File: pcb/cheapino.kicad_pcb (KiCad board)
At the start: 2 copper layers, 132.5 x 95.1 mm, 149 parts, among them J1 USB_C_Receptacle_USB2.0_16P, J2 DBG, J3 SJ-43514, K1 SW_Push, K10 SW_Push, K11 SW_Push, K12 SW_Push, K13 SW_Push, K14 SW_Push, K15 SW_Push, K16 SW_Push, K17 SW_Push, K18 SW_Push, K2 SW_Push, K3 SW_Push, K4 SW_Push, K5 SW_Push, K6 SW_Push, K7 SW_Push, K8 SW_Push, K9 SW_Push, SW1 BOOT, SW2 RST, U1 RP2040, U2 W25Q128JVSIQ, U3 AP2112K-3.3, U4 TVS0500DRV, U5 TPD2E2U06, U6 TPD2E2U06, U7 TXS0101DBV, U8 TXS0101DBV, Y1 12MHz

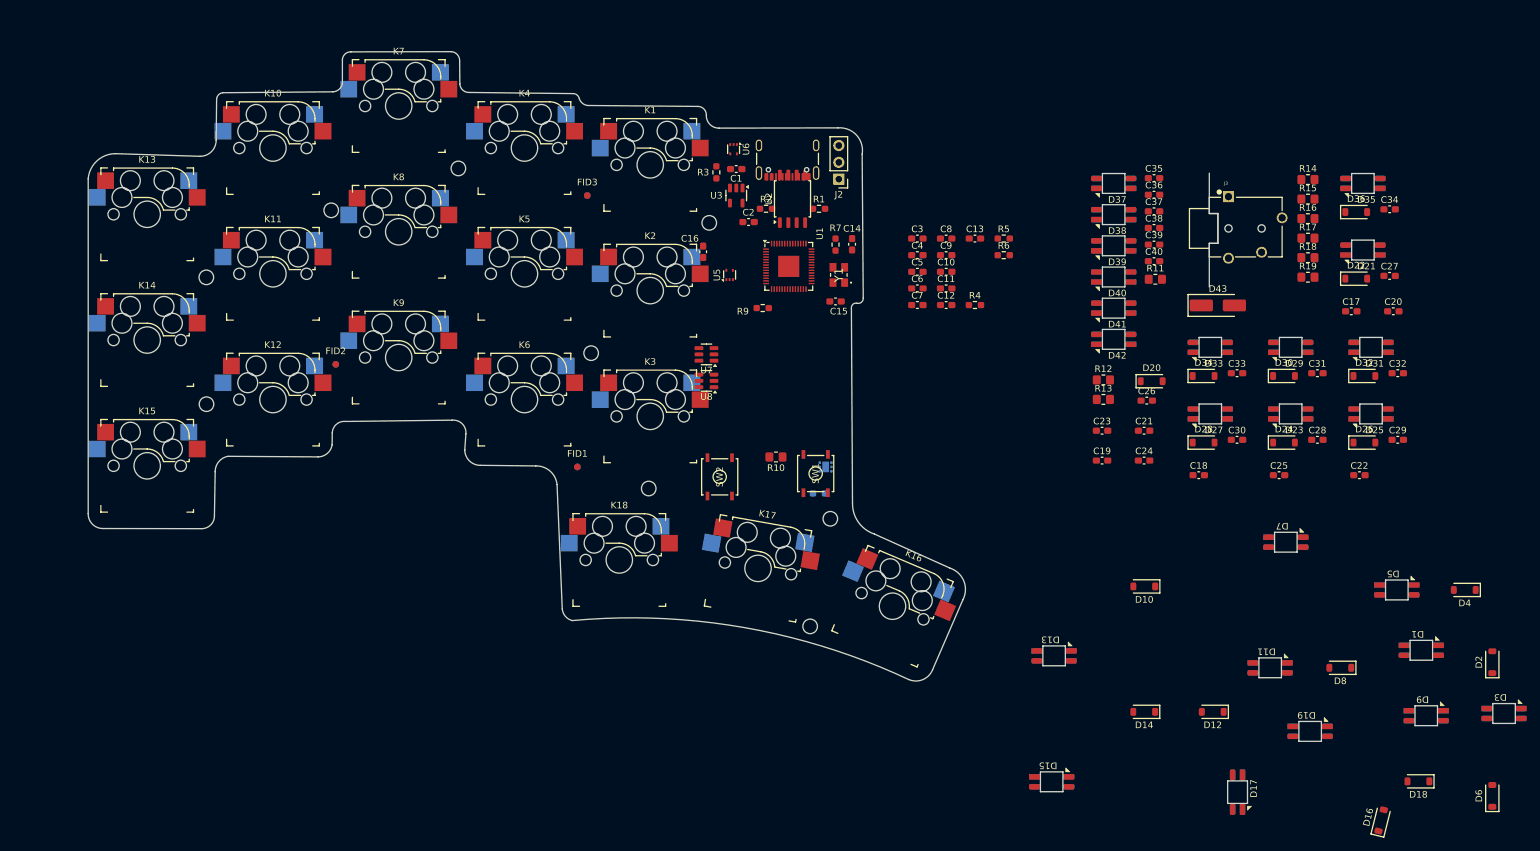
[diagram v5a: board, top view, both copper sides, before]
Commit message: Broke out Underglow LEDs into a common hierarchical sheet for what may be more consistent placements. Additionally created hierarchical PCB layouts and started using the HierarchicalPcb plugin (https://github.com/gauravmm/HierarchicalPcb.git) to automatically layout repeated components for the keymap.
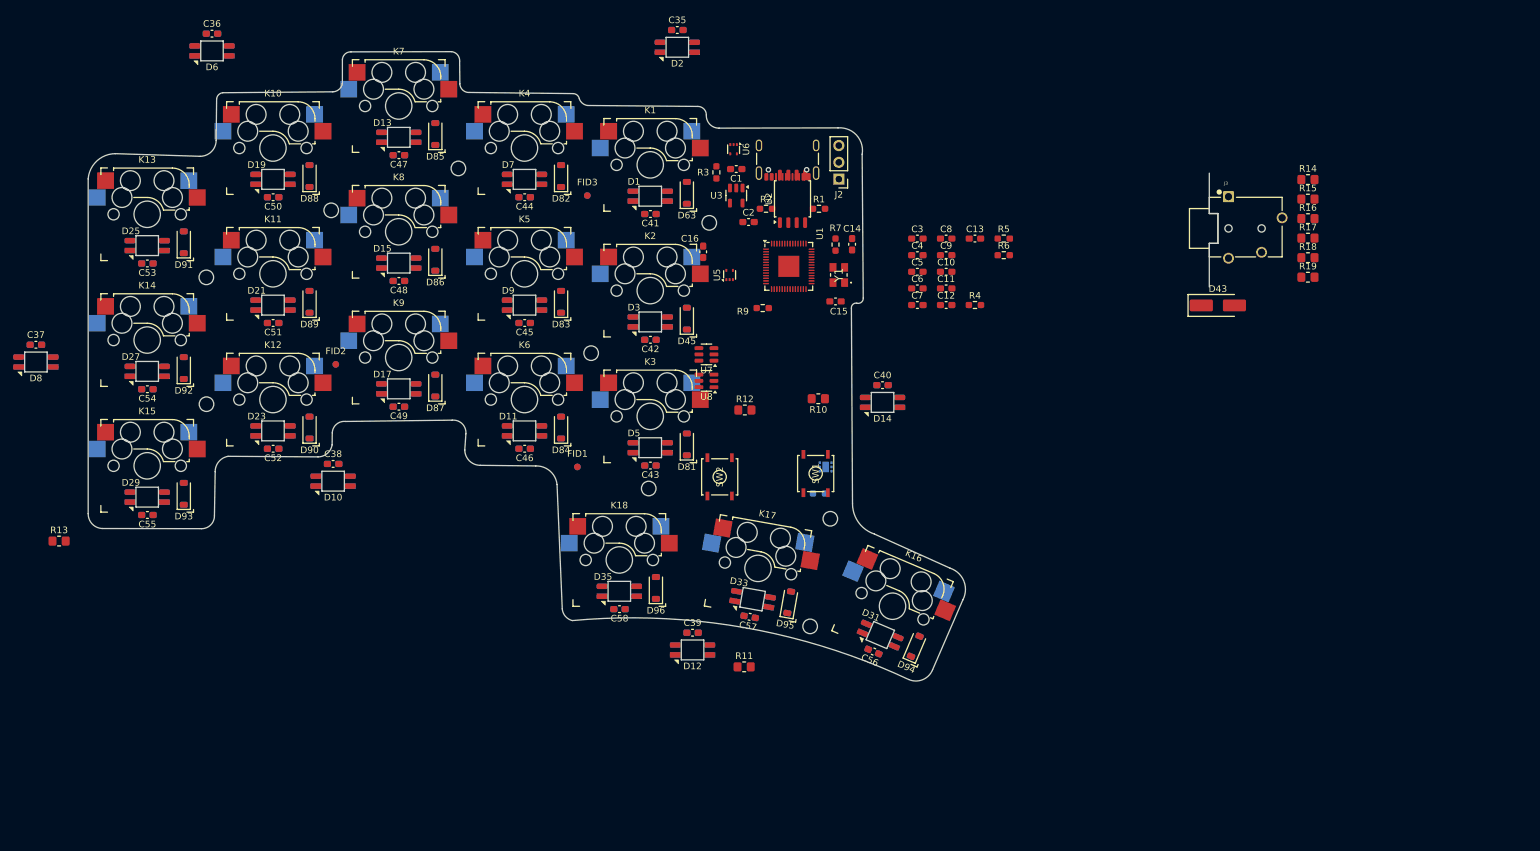
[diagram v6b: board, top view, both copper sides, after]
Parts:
- removed D16, D18, D20, D22, D24, D26, D28, D30, D32, D34, D36: 1N4148W, Diode_SMD:D_SOD-123
- removed D37, D38, D39, D40, D41, D42: ~, Extra:SK6812-MINI-E_ReverseMount_reversible
- added C41: 100nF, Capacitor_SMD:C_0603_1608Metric_Pad1.08x0.95mm_HandSolder, F.Cu at (145.0, 70.3)
- added C42: 100nF, Capacitor_SMD:C_0603_1608Metric_Pad1.08x0.95mm_HandSolder, F.Cu at (145.0, 89.3)
- added C43: 100nF, Capacitor_SMD:C_0603_1608Metric_Pad1.08x0.95mm_HandSolder, F.Cu at (145.0, 108.3)
- added C44: 100nF, Capacitor_SMD:C_0603_1608Metric_Pad1.08x0.95mm_HandSolder, F.Cu at (126.0, 67.8)
- added C45: 100nF, Capacitor_SMD:C_0603_1608Metric_Pad1.08x0.95mm_HandSolder, F.Cu at (126.0, 86.8)
- added C46: 100nF, Capacitor_SMD:C_0603_1608Metric_Pad1.08x0.95mm_HandSolder, F.Cu at (126.0, 105.8)
- added C47: 100nF, Capacitor_SMD:C_0603_1608Metric_Pad1.08x0.95mm_HandSolder, F.Cu at (107.0, 61.4)
- added C48: 100nF, Capacitor_SMD:C_0603_1608Metric_Pad1.08x0.95mm_HandSolder, F.Cu at (107.0, 80.4)
- added C49: 100nF, Capacitor_SMD:C_0603_1608Metric_Pad1.08x0.95mm_HandSolder, F.Cu at (107.0, 99.4)
- added C50: 100nF, Capacitor_SMD:C_0603_1608Metric_Pad1.08x0.95mm_HandSolder, F.Cu at (88.0, 67.8)
- added C51: 100nF, Capacitor_SMD:C_0603_1608Metric_Pad1.08x0.95mm_HandSolder, F.Cu at (88.0, 86.8)
- added C52: 100nF, Capacitor_SMD:C_0603_1608Metric_Pad1.08x0.95mm_HandSolder, F.Cu at (88.0, 105.8)
- added C53: 100nF, Capacitor_SMD:C_0603_1608Metric_Pad1.08x0.95mm_HandSolder, F.Cu at (69.0, 77.8)
- added C54: 100nF, Capacitor_SMD:C_0603_1608Metric_Pad1.08x0.95mm_HandSolder, F.Cu at (69.0, 96.8)
- added C55: 100nF, Capacitor_SMD:C_0603_1608Metric_Pad1.08x0.95mm_HandSolder, F.Cu at (69.0, 115.8)
- added C56: 100nF, Capacitor_SMD:C_0603_1608Metric_Pad1.08x0.95mm_HandSolder, F.Cu at (178.7, 136.4)
- added C57: 100nF, Capacitor_SMD:C_0603_1608Metric_Pad1.08x0.95mm_HandSolder, F.Cu at (160.0, 131.1)
- added C58: 100nF, Capacitor_SMD:C_0603_1608Metric_Pad1.08x0.95mm_HandSolder, F.Cu at (140.4, 130.0)
- added C59: 100nF, Capacitor_SMD:C_0603_1608Metric_Pad1.08x0.95mm_HandSolder, B.Cu at (149.1, 42.5)
- added C60: 100nF, Capacitor_SMD:C_0603_1608Metric_Pad1.08x0.95mm_HandSolder, B.Cu at (78.8, 43.0)
- added C61: 100nF, Capacitor_SMD:C_0603_1608Metric_Pad1.08x0.95mm_HandSolder, B.Cu at (52.2, 90.0)
- added C62: 100nF, Capacitor_SMD:C_0603_1608Metric_Pad1.08x0.95mm_HandSolder, B.Cu at (97.1, 108.0)
- added C63: 100nF, Capacitor_SMD:C_0603_1608Metric_Pad1.08x0.95mm_HandSolder, B.Cu at (151.4, 133.5)
- added C65: 100nF, Capacitor_SMD:C_0603_1608Metric_Pad1.08x0.95mm_HandSolder, B.Cu at (180.1, 96.1)
- added D45: 1N4148W, Diode_SMD:D_SOD-123, F.Cu at (150.5, 86.1)
- added D62: 1N4148W, Diode_SMD:D_SOD-123, B.Cu at (150.5, 67.1)
- added D63: 1N4148W, Diode_SMD:D_SOD-123, F.Cu at (150.5, 67.1)
- added D64: 1N4148W, Diode_SMD:D_SOD-123, B.Cu at (150.5, 105.1)
- added D65: 1N4148W, Diode_SMD:D_SOD-123, B.Cu at (131.5, 64.6)
- added D66: 1N4148W, Diode_SMD:D_SOD-123, B.Cu at (131.5, 83.6)
- added D67: 1N4148W, Diode_SMD:D_SOD-123, B.Cu at (131.5, 102.6)
- added D68: 1N4148W, Diode_SMD:D_SOD-123, B.Cu at (112.5, 58.2)
- added D69: 1N4148W, Diode_SMD:D_SOD-123, B.Cu at (112.5, 77.2)
- added D70: 1N4148W, Diode_SMD:D_SOD-123, B.Cu at (112.5, 96.2)
- added D71: 1N4148W, Diode_SMD:D_SOD-123, B.Cu at (93.5, 64.6)
- added D72: 1N4148W, Diode_SMD:D_SOD-123, B.Cu at (93.5, 83.6)
- added D73: 1N4148W, Diode_SMD:D_SOD-123, B.Cu at (93.5, 102.6)
- added D74: 1N4148W, Diode_SMD:D_SOD-123, B.Cu at (74.5, 74.6)
- added D75: 1N4148W, Diode_SMD:D_SOD-123, B.Cu at (74.5, 93.6)
- added D76: 1N4148W, Diode_SMD:D_SOD-123, B.Cu at (74.5, 112.6)
- added D77: 1N4148W, Diode_SMD:D_SOD-123, B.Cu at (185.0, 135.6)
- added D78: 1N4148W, Diode_SMD:D_SOD-123, B.Cu at (166.0, 129.0)
- added D79: 1N4148W, Diode_SMD:D_SOD-123, B.Cu at (145.9, 126.8)
- added D81: 1N4148W, Diode_SMD:D_SOD-123, F.Cu at (150.5, 105.1)
- added D82: 1N4148W, Diode_SMD:D_SOD-123, F.Cu at (131.5, 64.6)
- added D83: 1N4148W, Diode_SMD:D_SOD-123, F.Cu at (131.5, 83.6)
- added D84: 1N4148W, Diode_SMD:D_SOD-123, F.Cu at (131.5, 102.6)
- added D85: 1N4148W, Diode_SMD:D_SOD-123, F.Cu at (112.5, 58.2)
- added D86: 1N4148W, Diode_SMD:D_SOD-123, F.Cu at (112.5, 77.2)
- added D87: 1N4148W, Diode_SMD:D_SOD-123, F.Cu at (112.5, 96.2)
- added D88: 1N4148W, Diode_SMD:D_SOD-123, F.Cu at (93.5, 64.6)
- added D89: 1N4148W, Diode_SMD:D_SOD-123, F.Cu at (93.5, 83.6)
- added D90: 1N4148W, Diode_SMD:D_SOD-123, F.Cu at (93.5, 102.6)
- added D91: 1N4148W, Diode_SMD:D_SOD-123, F.Cu at (74.5, 74.6)
- added D92: 1N4148W, Diode_SMD:D_SOD-123, F.Cu at (74.5, 93.6)
- added D93: 1N4148W, Diode_SMD:D_SOD-123, F.Cu at (74.5, 112.6)
- added D94: 1N4148W, Diode_SMD:D_SOD-123, F.Cu at (185.0, 135.6)
- added D95: 1N4148W, Diode_SMD:D_SOD-123, F.Cu at (166.0, 129.0)
- added D96: 1N4148W, Diode_SMD:D_SOD-123, F.Cu at (145.9, 126.8)
- C17, C18, C19, C20, C21, C22, C23, C24, C25, C26, C27, C28, C29, C30, C31, C32, C33, C34, D4: moved to B.Cu
- D10, D12, D14, D2, D6, D8: value 1N4148W -> ~; footprint Diode_SMD:D_SOD-123 -> Extra:SK6812-MINI-E_ReverseMount_reversible
- moved D6 223.8 mm to (78.8, 45.6), turned to 0 degrees
- moved D8 202.4 mm to (52.2, 92.7), turned to 0 degrees
- moved C29 190.8 mm to (69.0, 77.8)
- moved D25 186.6 mm to (69.0, 75.1)
- moved C31 178.1 mm to (69.0, 115.8)
- moved D19 177.5 mm to (88.0, 65.1), turned to 0 degrees
- moved D29 174.2 mm to (69.0, 113.1)
- moved C37 170.1 mm to (52.2, 90.0), turned to 180 degrees
- moved C27 168.8 mm to (88.0, 86.8)
- moved D21 164.9 mm to (88.0, 84.1)
- moved C30 164.8 mm to (69.0, 96.8)
- moved D27 160.7 mm to (69.0, 94.1)
- moved R13 159.2 mm to (55.7, 119.7)
- moved C28 157.8 mm to (88.0, 105.8)
- moved D2 154.2 mm to (149.1, 45.1), turned to 0 degrees
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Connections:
- D10 pad 1: Net-(D10-K) -> GND
- D10 pad 2: /KeySwitches/ROW_1 -> /Lighting/Underglow_LED2/DOUT
- D12 pad 1: Net-(D12-K) -> GND
- D12 pad 2: /KeySwitches/ROW_1 -> /Lighting/Underglow_LED3/DOUT
- D14 pad 1: Net-(D14-K) -> GND
- D14 pad 2: /KeySwitches/ROW_2 -> /Lighting/Underglow_LED4/DOUT
- D2 pad 1: Net-(D2-K) -> GND
- D2 pad 2: /KeySwitches/ROW_1 -> /Lighting/Underglow_LED0/DIN
- D4 pad 1: Net-(D4-K) -> /KeySwitches/ROW_1
- D4 pad 2: /KeySwitches/ROW_1 -> Net-(D4-A)
- D6 pad 1: Net-(D6-K) -> GND
- D6 pad 2: /KeySwitches/ROW_1 -> /Lighting/Underglow_LED0/DOUT
- D8 pad 1: Net-(D8-K) -> GND
- D8 pad 2: /KeySwitches/ROW_1 -> /Lighting/Underglow_LED1/DOUT
- K1 pad 2: Net-(D2-K) -> Net-(D62-A)
- K2 pad 2: Net-(D4-K) -> Net-(D4-A)
- K3 pad 2: Net-(D6-K) -> Net-(D64-A)
- K4 pad 2: Net-(D8-K) -> Net-(D65-A)
- K5 pad 2: Net-(D10-K) -> Net-(D66-A)
- K6 pad 2: Net-(D12-K) -> Net-(D67-A)
- K7 pad 2: Net-(D14-K) -> Net-(D68-A)
- R10 pad 1: Net-(D37-DIN) -> /Lighting/Underglow_LED0/DIN
- R11 pad 2: Net-(D42-DOUT) -> /Lighting/Underglow_LED5/DOUT
- U5 pad 1: GND -> unconnected-(U5-NC-Pad1)
- U5 pad 2: GND -> unconnected-(U5-NC-Pad2)
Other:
- board text removed: "Solder on right side only"

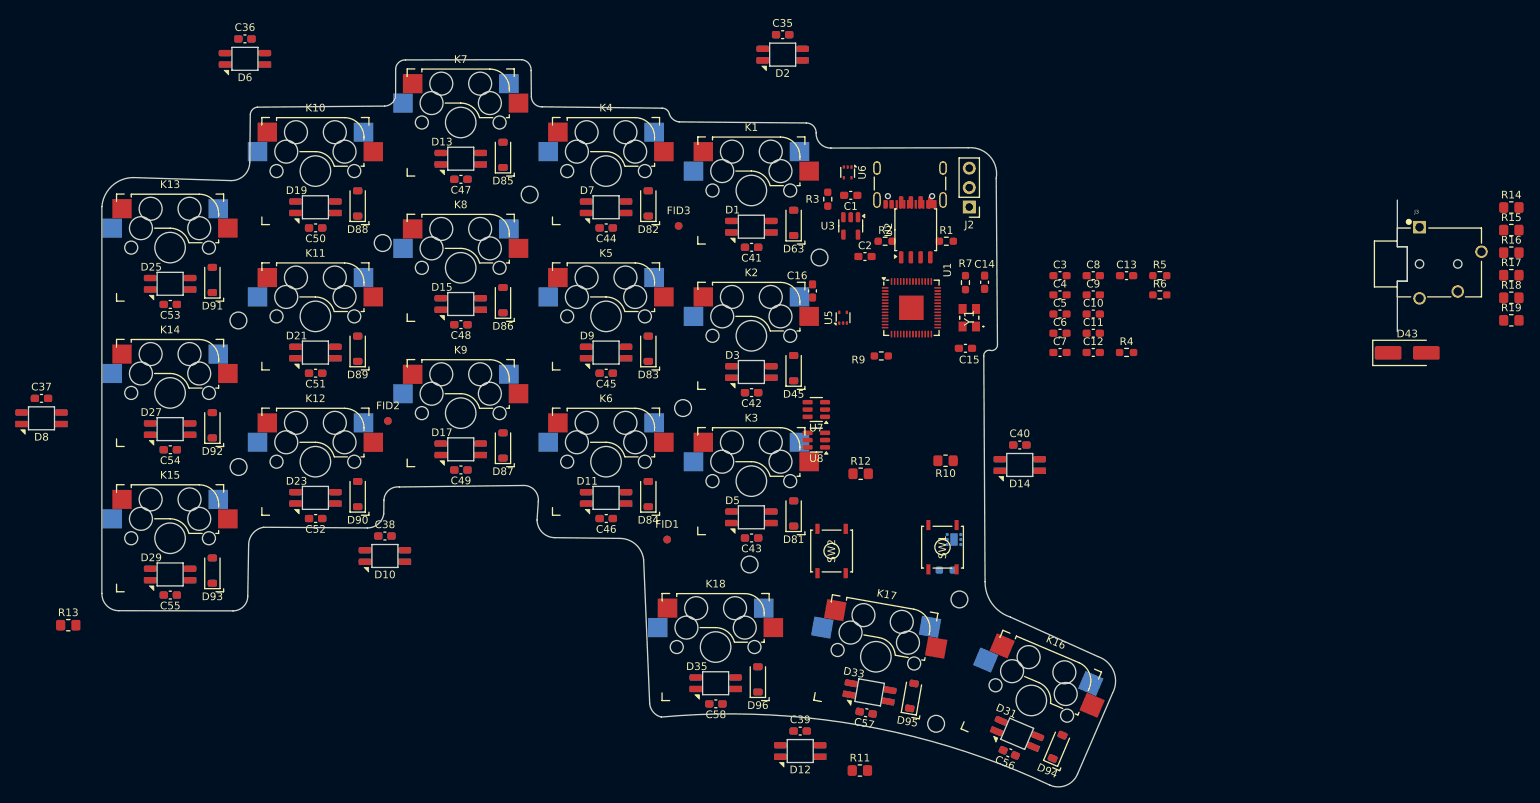
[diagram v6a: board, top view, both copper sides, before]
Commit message: Renumbering all reference designations and adding an initial layout for each keyswtich sub-pcb.
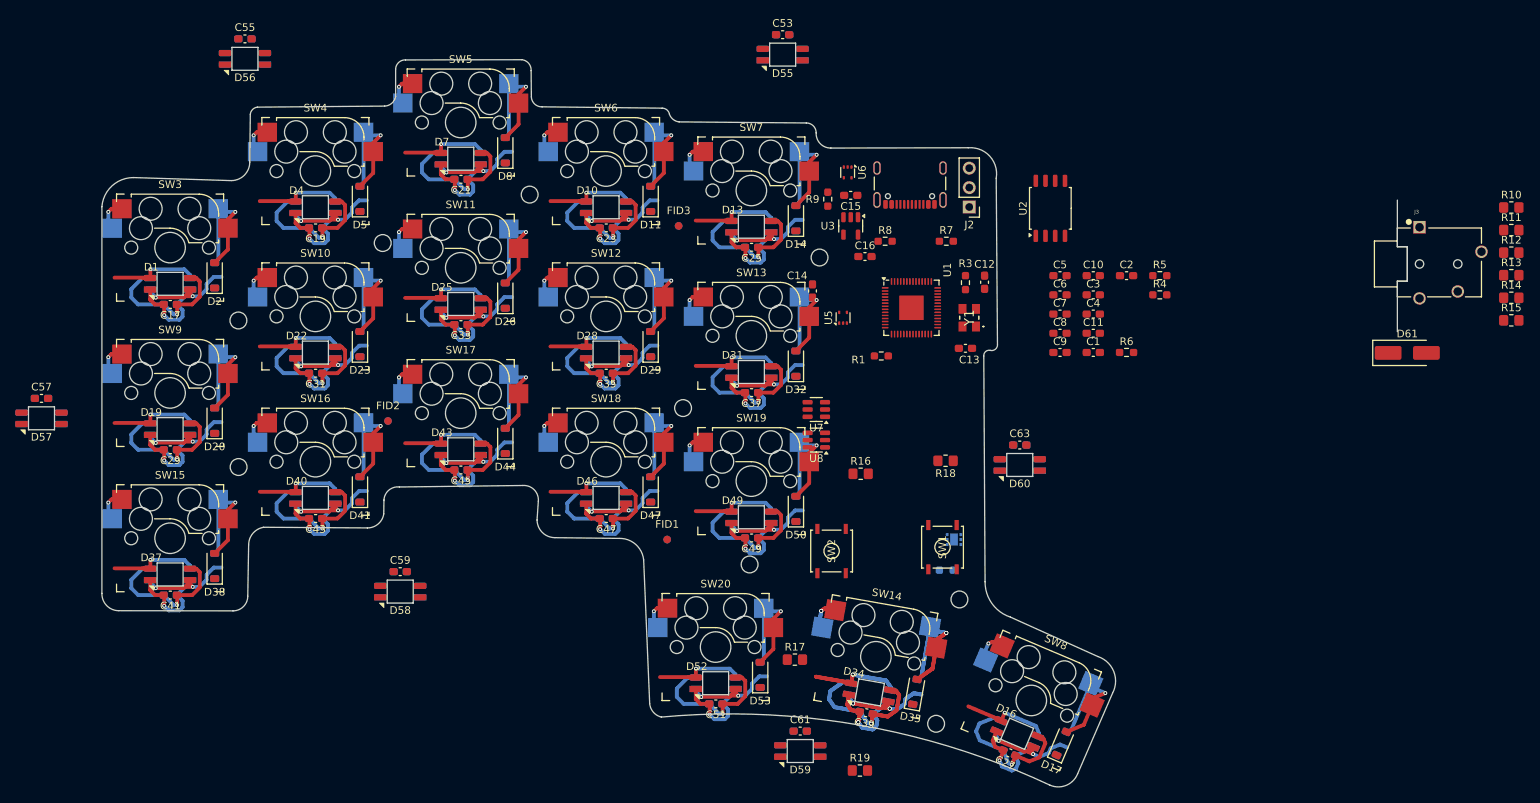
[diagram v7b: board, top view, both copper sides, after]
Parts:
- removed the C23 at (107.0, 61.4)
- removed the C32 at (178.7, 136.4)
- removed the C42 at (145.0, 89.3)
- removed the C56 at (178.7, 136.4)
- removed the D13 at (107.0, 58.7)
- removed the D31 at (179.8, 133.9)
- removed the D45 at (150.5, 86.1)
- removed D68, D77, D85, D94: 1N4148W, Diode_SMD:D_SOD-123
- removed K16, K2, K7: SW_Push, Extra:Kailh_socket_MX_reversible
- added C17: 100nF, Capacitor_SMD:C_0603_1608Metric_Pad1.08x0.95mm_HandSolder, F.Cu at (69.0, 77.8)
- added C39: 100nF, Capacitor_SMD:C_0603_1608Metric_Pad1.08x0.95mm_HandSolder, F.Cu at (160.0, 131.1)
- added C40: 100nF, Capacitor_SMD:C_0603_1608Metric_Pad1.08x0.95mm_HandSolder, B.Cu at (160.0, 131.1)
- added C48: 100nF, Capacitor_SMD:C_0603_1608Metric_Pad1.08x0.95mm_HandSolder, B.Cu at (126.0, 105.8)
- added D2: 1N4148W, Diode_SMD:D_SOD-123, F.Cu at (74.8, 74.0)
- added D34: ~, Extra:SK6812-MINI-E_ReverseMount_reversible, F.Cu at (160.5, 128.5)
- added D35: 1N4148W, Diode_SMD:D_SOD-123, F.Cu at (166.4, 128.4)
- added D36: 1N4148W, Diode_SMD:D_SOD-123, B.Cu at (166.4, 128.4)
- added D46: ~, Extra:SK6812-MINI-E_ReverseMount_reversible, F.Cu at (126.0, 103.1)
- added D47: 1N4148W, Diode_SMD:D_SOD-123, F.Cu at (131.8, 102.0)
- added D48: 1N4148W, Diode_SMD:D_SOD-123, B.Cu at (131.8, 102.0)
- added SW14: CPG151101S11, Extra:Kailh_socket_MX_reversible, F.Cu at (161.3, 123.8)
- added SW18: CPG151101S11, Extra:Kailh_socket_MX_reversible, F.Cu at (126.0, 98.3)
- added SW3: CPG151101S11, Extra:Kailh_socket_MX_reversible, F.Cu at (69.0, 70.3)
- SW10: renamed from K11; value SW_Push -> CPG151101S11
- SW11: renamed from K9; value SW_Push -> CPG151101S11
- SW12: renamed from K10; value SW_Push -> CPG151101S11
- SW13: renamed from K8; value SW_Push -> CPG151101S11
- SW15: renamed from K18; value SW_Push -> CPG151101S11
- SW16: renamed from K17; value SW_Push -> CPG151101S11
- SW17: renamed from K15; value SW_Push -> CPG151101S11
- SW19: renamed from K14; value SW_Push -> CPG151101S11
- SW20: renamed from K13; value SW_Push -> CPG151101S11
- SW4: renamed from K1; value SW_Push -> CPG151101S11
- SW5: renamed from K3; value SW_Push -> CPG151101S11
- SW6: renamed from K4; value SW_Push -> CPG151101S11
- SW7: renamed from K5; value SW_Push -> CPG151101S11
- SW8: renamed from K6; value SW_Push -> CPG151101S11
- SW9: renamed from K12; value SW_Push -> CPG151101S11
- moved R17 95.1 mm to (150.7, 124.2)
- moved C51 88.4 mm to (140.4, 130.0)
- moved C52 88.4 mm to (140.4, 130.0)
- moved SW20 88.4 mm to (140.3, 122.6)
- moved D52 88.4 mm to (140.3, 127.3)
- moved D53 88.3 mm to (146.2, 126.2)
- moved D54 88.3 mm to (146.2, 126.2)
- moved SW16 77.6 mm to (88.0, 98.3), turned to 0 degrees
- moved D50 77.1 mm to (150.8, 104.5)
- moved D51 77.1 mm to (150.8, 104.5)
- moved D41 77.0 mm to (93.8, 102.0), turned to 90 degrees
- moved D42 77.0 mm to (93.8, 102.0), turned to 90 degrees
- moved C18 76.9 mm to (69.0, 77.8)
- moved C49 76.9 mm to (145.0, 108.3)
- moved C50 76.9 mm to (145.0, 108.3)
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- renumbered C12 to C1, C8 to C10, C14 to C12, C15 to C13, C16 to C14, C1 to C15, C2 to C16, C41 to C19, C13 to C2, C17 to C20, C43 to C21, C19 to C22, C44 to C23, C20 to C24, C45 to C25, C21 to C26, C46 to C27, C22 to C28, C52 to C29, C9 to C3, C28 to C30, C51 to C31, C27 to C32, C49 to C33, C25 to C34, C50 to C35, C26 to C36, C48 to C37, C24 to C38, C10 to C4, C58 to C41, C34 to C42, C57 to C43, C33 to C44, C55 to C45, C31 to C46, C54 to C49, C3 to C5, C30 to C50, C53 to C51, C29 to C52, C35 to C53, C59 to C54, C36 to C55, C60 to C56, C37 to C57, C61 to C58, C38 to C59, C4 to C6, C62 to C60, C39 to C61, C63 to C62, C40 to C63, C65 to C64, C5 to C7, C6 to C8, C7 to C9, D3 to D1, D7 to D10, D82 to D11, D65 to D12, D9 to D13, D83 to D14, D66 to D15, D11 to D16, D84 to D17, D67 to D18, D23 to D19, D90 to D20, D73 to D21, D21 to D22, D89 to D23, D72 to D24, D17 to D25, D87 to D26, D70 to D27, D19 to D28, D88 to D29, D4 to D3, D71 to D30, D15 to D31, D86 to D32, D69 to D33, D35 to D37, D96 to D38, D79 to D39, D1 to D4, D33 to D40, D95 to D41, D78 to D42, D29 to D43, D93 to D44, D76 to D45, D27 to D49, D63 to D5, D92 to D50, D75 to D51, D25 to D52, D91 to D53, D74 to D54, D2 to D55, D6 to D56, D8 to D57, D10 to D58, D12 to D59, D62 to D6, D14 to D60, D43 to D61, D5 to D7, D81 to D8, D64 to D9, R9 to R1, R14 to R10, R15 to R11, R16 to R12, R17 to R13, R18 to R14, R19 to R15, R12 to R16, R13 to R17, R10 to R18, R11 to R19, R8 to R2, R7 to R3, R6 to R4, R4 to R6, R1 to R7, R2 to R8, R3 to R9
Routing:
- net VSYS: track 0.00 -> 366.1 mm, vias 0 -> 19
- net GND: track 0.00 -> 230.9 mm, vias 0 -> 19
- net /KeySwitches/KeySwitch_RGB_1_2/LED_Out: track 0.00 -> 39.4 mm, vias 0 -> 5
- net /KeySwitches/KeySwitch_RGB_1_2/LED_In: track 0.00 -> 37.4 mm, vias 0 -> 4
- net /KeySwitches/ROW_3: track 0.00 -> 34.9 mm, vias 0 -> 2
- net /KeySwitches/COL_5: track 0.00 -> 30.3 mm, vias 0 -> 4
- net /KeySwitches/KeySwitch_RGB_4_2/LED_In: track 0.00 -> 25.6 mm, vias 0 -> 3
- net /KeySwitches/KeySwitch_RGB_2_2/LED_In: track 0.00 -> 25.6 mm, vias 0 -> 3
- net /KeySwitches/KeySwitch_RGB_2_3/LED_Out: track 0.00 -> 25.6 mm, vias 0 -> 3
- net /KeySwitches/KeySwitch_RGB_6_1/LED_Out: track 0.00 -> 25.6 mm, vias 0 -> 3
- net /KeySwitches/KeySwitch_RGB_5_2/LED_In: track 0.00 -> 25.6 mm, vias 0 -> 3
- net /KeySwitches/KeySwitch_RGB_1_3/LED_Out: track 0.00 -> 25.6 mm, vias 0 -> 3
- net /KeySwitches/KeySwitch_RGB_3_1/LED_Out: track 0.00 -> 25.6 mm, vias 0 -> 3
- net /KeySwitches/KeySwitch_RGB_5_1/LED_Out: track 0.00 -> 25.6 mm, vias 0 -> 3
- net /KeySwitches/KeySwitch_RGB_3_3/LED_Out: track 0.00 -> 25.6 mm, vias 0 -> 3
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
